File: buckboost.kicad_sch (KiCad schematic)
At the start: 17 parts, among them Q1 AO3401A, Q2 AO3401A, Q3 AO3400A, Q4 AO3400A, U4 IRS2003, U5 IRS2003

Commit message: More layout adust
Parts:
- removed C14, C15: 10u, Capacitor_SMD:C_0805_2012Metric, symbol Device:C

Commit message: Routing more
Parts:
- renumbered TP5 to TP_A, TP6 to TP_B
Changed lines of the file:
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@@
 		(dnp no)
 		(fields_autoplaced yes)
-		(property "Reference" "TP5"
-			(at 158.75 80.5179 0)
+		(property "Reference" "TP_A"
+			(at 158.75 81.7879 0)
 			(effects
 				(font
@@
 			(project "JPBms2"
 				(path "/d86e471c-a8be-422d-a5d1-5a4699b7b766/0f5ad211-c4ad-40eb-a8ac-82970ee8fac9"
-					(reference "TP5")
+					(reference "TP_A")
 					(unit 1)
 				)
@@
 		(dnp no)
 		(fields_autoplaced yes)
-		(property "Reference" "TP6"
-			(at 186.69 80.5179 0)
+		(property "Reference" "TP_B"
+			(at 186.69 81.7879 0)
 			(effects
 				(font
@@
 			(project "JPBms2"
 				(path "/d86e471c-a8be-422d-a5d1-5a4699b7b766/0f5ad211-c4ad-40eb-a8ac-82970ee8fac9"
-					(reference "TP6")
-					(unit 1)
-				)
+					(reference "TP_B")
+					(unit 1)
+				)

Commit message: Routing
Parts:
- renumbered TP_A to TP5, TP_B to TP6
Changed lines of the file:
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@@
 		(dnp no)
 		(fields_autoplaced yes)
-		(property "Reference" "TP_A"
+		(property "Reference" "TP5"
 			(at 158.75 81.7879 0)
 			(effects
@@
 				)
 				(justify left)
-				(hide yes)
 			)
 		)
@@
 			(project "JPBms2"
 				(path "/d86e471c-a8be-422d-a5d1-5a4699b7b766/0f5ad211-c4ad-40eb-a8ac-82970ee8fac9"
-					(reference "TP_A")
+					(reference "TP5")
 					(unit 1)
 				)
@@
 		(dnp no)
 		(fields_autoplaced yes)
-		(property "Reference" "TP_B"
+		(property "Reference" "TP6"
 			(at 186.69 81.7879 0)
 			(effects
@@
 				)
 				(justify left)
-				(hide yes)
 			)
 		)
@@
 			(project "JPBms2"
 				(path "/d86e471c-a8be-422d-a5d1-5a4699b7b766/0f5ad211-c4ad-40eb-a8ac-82970ee8fac9"
-					(reference "TP_B")
-					(unit 1)
-				)
+					(reference "TP6")
+					(unit 1)
+				)

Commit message: Assigning PNs
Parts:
- L1: value 220uH -> 22uH; LCSC_Code (none) -> C497873
- Q1, Q2: LCSC_Code (none) -> C15127
- Q3, Q4: LCSC_Code (none) -> C20917
- R11, R12, R13, R14: value 50 -> 75; LCSC_Code (none) -> C4275
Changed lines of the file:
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@@
 			)
 		)
-		(property "Value" "50"
+		(property "Value" "75"
 			(at 77.47 105.41 90)
 			(effects
@@
 			)
 		)
+		(property "LCSC_Code" "C4275"
+			(at 77.47 109.22 0)
+			(effects
+				(font
+					(size 1.27 1.27)
+				)
+				(hide yes)
+			)
+		)
 		(pin "1"
 		)
@@
 			)
 		)
-		(property "Value" "220uH"
+		(property "Value" "22uH"
 			(at 170.18 82.55 90)
 			(effects
@@
 			)
 		)
+		(property "LCSC_Code" "C497873"
+			(at 170.18 85.09 0)
+			(effects
+				(font
+					(size 1.27 1.27)
+				)
+				(hide yes)
+			)
+		)
 		(pin "2"
 		)
@@
 			)
 		)
-		(property "Value" "50"
+		(property "Value" "75"
 			(at 77.47 49.53 90)
 			(effects
@@
 			)
 		)
+		(property "LCSC_Code" "C4275"
+			(at 77.47 53.34 0)
+			(effects
+				(font
+					(size 1.27 1.27)
+				)
+				(hide yes)
+			)
+		)
 		(pin "1"
 		)
@@
 			)
 		)
+		(property "LCSC_Code" "C20917"
+			(at 142.24 93.98 0)
+			(effects
+				(font
+					(size 1.27 1.27)
+				)
+				(hide yes)
+			)
+		)
 		(pin "2"
 		)
@@
 			)
 		)
-		(property "Value" "50"
+		(property "Value" "75"
 			(at 77.47 118.11 90)
 			(effects
@@
 			)
 		)
+		(property "LCSC_Code" "C4275"
+			(at 77.47 121.92 0)
+			(effects
+				(font
+					(size 1.27 1.27)
+				)
+				(hide yes)
+			)
+		)
 		(pin "1"
 		)
@@
 			)
 		)
+		(property "LCSC_Code" "C15127"
+			(at 194.31 73.66 0)
+			(effects
+				(font
+					(size 1.27 1.27)
+				)
+				(hide yes)
+			)
+		)
 		(pin "3"
 		)
@@
 			)
 		)
+		(property "LCSC_Code" "C15127"
+			(at 142.24 73.66 0)
+			(effects
+				(font
+					(size 1.27 1.27)
+				)
+				(hide yes)
+			)
+		)
 		(pin "3"
 		)
@@
 			)
 		)
+		(property "LCSC_Code" "C20917"
+			(at 194.31 93.98 0)
+			(effects
+				(font
+					(size 1.27 1.27)
+				)
+				(hide yes)
+			)
+		)
 		(pin "2"
 		)
@@
 			)
 		)
-		(property "Value" "50"
+		(property "Value" "75"
 			(at 77.47 62.23 90)
 			(effects
@@
 			(at 77.47 66.04 0)
 			(effects
+				(font
+					(size 1.27 1.27)
+				)
+				(hide yes)
+			)
+		)
+		(property "LCSC_Code" "C4275"
+			(at 77.47 66.04 0)
+			(effects

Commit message: slight changes
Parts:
- C16, C17: value .1u -> 1u; LCSC_Code C14663 -> C15849
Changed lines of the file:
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@@
 		(fields_autoplaced yes)
 		(property "Reference" "C17"
-			(at 44.45 99.0537 90)
-			(effects
-				(font
-					(size 1.27 1.27)
-				)
-			)
-		)
-		(property "Value" ".1u"
-			(at 46.99 99.0537 90)
-			(effects
-				(font
-					(size 1.27 1.27)
-				)
+			(at 53.34 97.7835 0)
+			(effects
+				(font
+					(size 1.27 1.27)
+				)
+				(justify right)
+			)
+		)
+		(property "Value" "1u"
+			(at 53.34 100.3235 0)
+			(effects
+				(font
+					(size 1.27 1.27)
+				)
+				(justify right)
 			)
 		)
@@
 			)
 		)
-		(property "LCSC_Code" "C14663"
+		(property "LCSC_Code" "C15849"
 			(at 50.8 99.06 0)
 			(effects
@@
 			)
 		)
-		(property "Value" ".1u"
+		(property "Value" "1u"
 			(at 45.72 43.1737 90)
 			(effects
@@
 			)
 		)
-		(property "LCSC_Code" "C14663"
+		(property "LCSC_Code" "C15849"
 			(at 49.53 43.18 0)
 			(effects

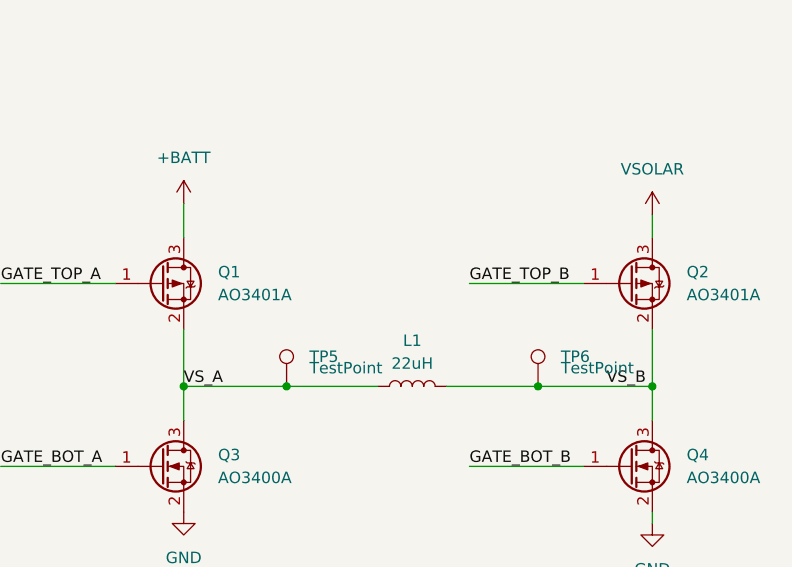
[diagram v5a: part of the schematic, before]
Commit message: Schematics updated P mosfets
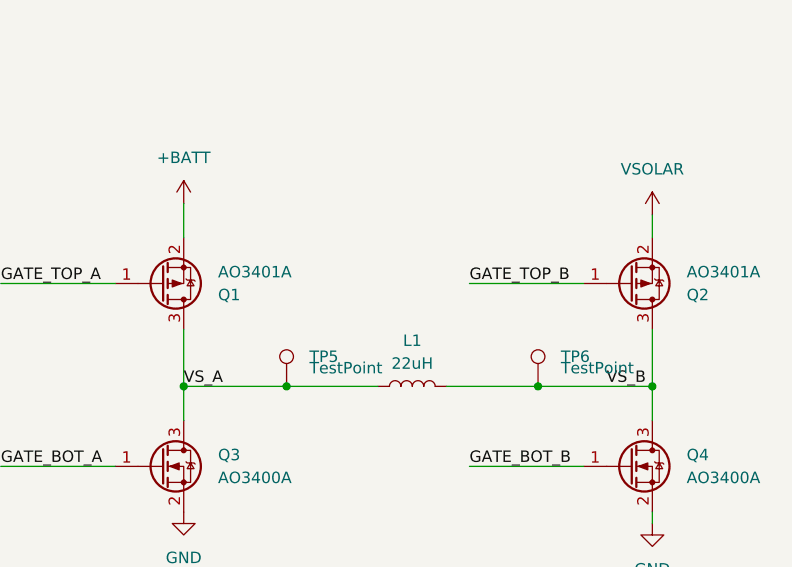
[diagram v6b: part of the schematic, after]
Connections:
- net +BATT: now also Q1.2 (S); no longer Q1.3 (D)
- net VSOLAR: now also Q2.2 (S); no longer Q2.3 (D)
- net VS_A: now also Q1.3 (D); no longer Q1.2 (S)
- net VS_B: now also Q2.3 (D); no longer Q2.2 (S)
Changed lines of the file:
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@@
 		(lib_id "Transistor_FET:AO3401A")
 		(at 194.31 73.66 0)
+		(mirror x)
 		(unit 1)
 		(exclude_from_sim no)
@@
 		(on_board yes)
 		(dnp no)
-		(fields_autoplaced yes)
 		(property "Reference" "Q2"
-			(at 200.66 72.3899 0)
+			(at 200.66 74.9301 0)
 			(effects
 				(font
@@
 		)
 		(property "Value" "AO3401A"
-			(at 200.66 74.9299 0)
+			(at 200.66 72.3901 0)
 			(effects
 				(font
@@
 		)
 		(property "Footprint" "Package_TO_SOT_SMD:SOT-23"
-			(at 199.39 75.565 0)
+			(at 199.39 71.755 0)
 			(effects
 				(font
@@
 		)
 		(property "Datasheet" "http://www.aosmd.com/pdfs/datasheet/AO3401A.pdf"
-			(at 199.39 77.47 0)
+			(at 199.39 69.85 0)
 			(effects
 				(font
@@
 		(lib_id "Transistor_FET:AO3401A")
 		(at 142.24 73.66 0)
+		(mirror x)
 		(unit 1)
 		(exclude_from_sim no)
@@
 		(on_board yes)
 		(dnp no)
-		(fields_autoplaced yes)
 		(property "Reference" "Q1"
-			(at 148.59 72.3899 0)
+			(at 148.59 74.9301 0)
 			(effects
 				(font
@@
 		)
 		(property "Value" "AO3401A"
-			(at 148.59 74.9299 0)
+			(at 148.59 72.3901 0)
 			(effects
 				(font
@@
 		)
 		(property "Footprint" "Package_TO_SOT_SMD:SOT-23"
-			(at 147.32 75.565 0)
+			(at 147.32 71.755 0)
 			(effects
 				(font
@@
 		)
 		(property "Datasheet" "http://www.aosmd.com/pdfs/datasheet/AO3401A.pdf"
-			(at 147.32 77.47 0)
+			(at 147.32 69.85 0)
 			(effects
 				(font

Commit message: New design and layout
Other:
- note added: "No bootstrap circuit, we use P-Fets on the high side, so you can just use VBATT, Practically, the bootstrap would run off of the low-side switches and let you use N-FEts. But I wanted to test this idea because it would let you control the duty cycle to any range (ex. for motor drives later). And we already had the P-FETs on the BOM"
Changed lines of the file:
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@@
+		)
+	)
+	(text "No bootstrap circuit, we use P-Fets on the high side, so you can just use VBATT,\n\nPractically, the bootstrap would run off of the low-side switches and let\nyou use N-FEts. But I wanted to test this idea because it would let you\ncontrol the duty cycle to any range (ex. for motor drives later).\nAnd we already had the P-FETs on the BOM"
+		(exclude_from_sim no)
+		(at 110.998 37.084 0)
+		(effects
+			(font
+				(size 1.27 1.27)
+			)
 		)
 	)

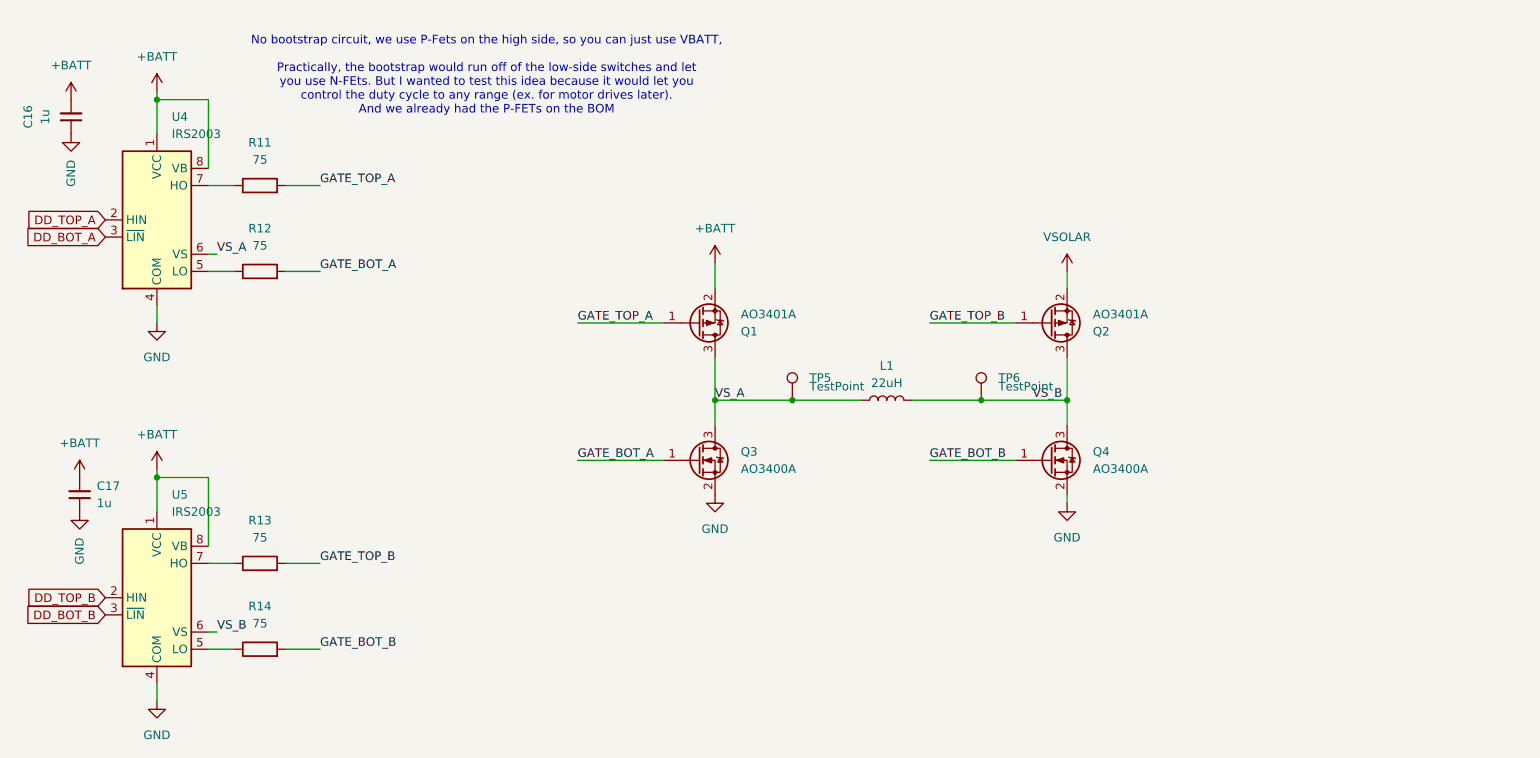
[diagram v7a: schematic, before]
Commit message: Better balance resistors, fixes
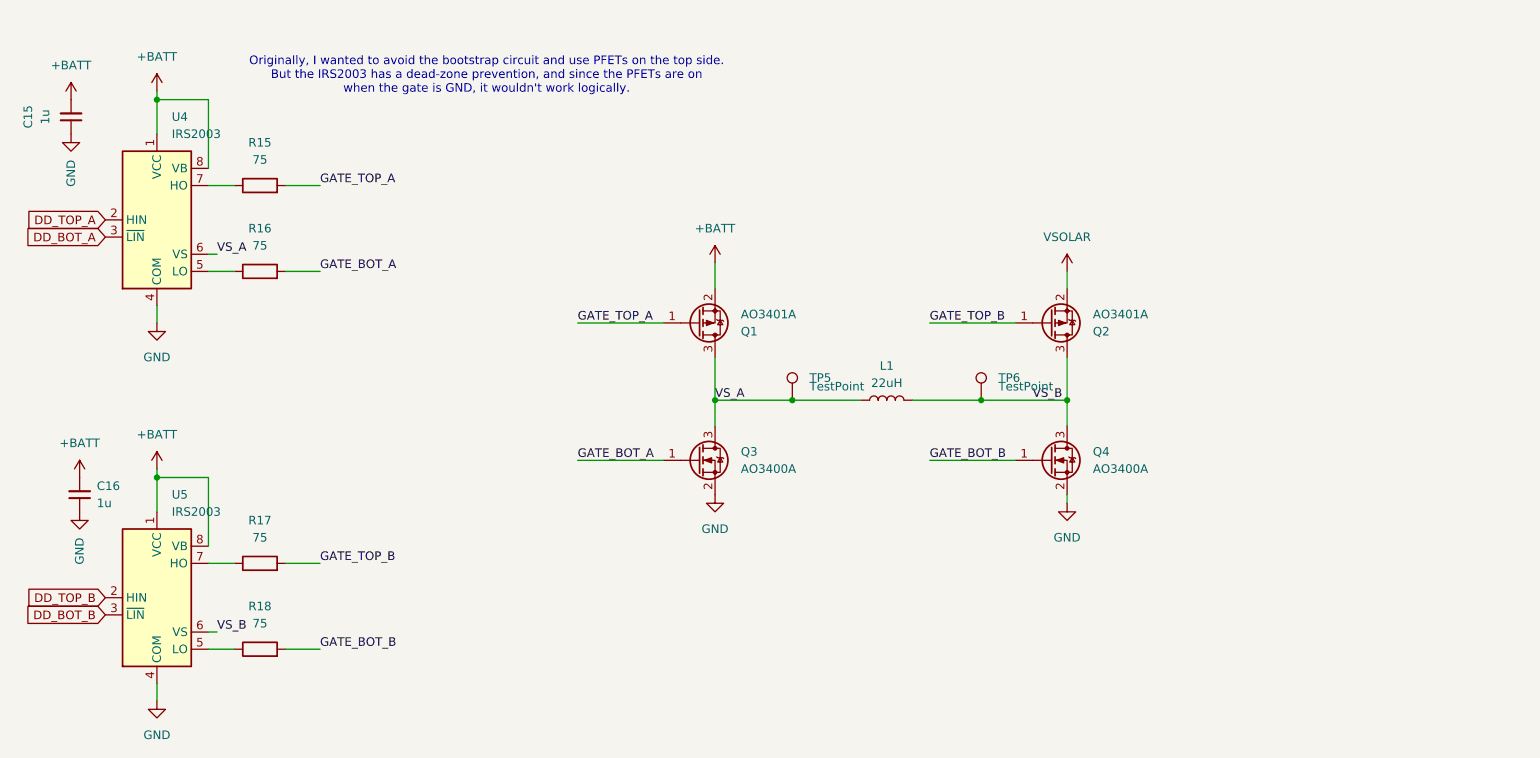
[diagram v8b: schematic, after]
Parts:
- renumbered C16 to C15, C17 to C16, R11 to R15, R12 to R16, R13 to R17, R14 to R18
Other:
- note added: "Originally, I wanted to avoid the bootstrap circuit and use PFETs on the top side. But the IRS2003 has a dead-zone prevention, and since the PFETs are on when the gate is GND, it wouldn't work logically."
- note removed: "No bootstrap circuit, we use P-Fets on the high side, so you can just use VBATT, Practically, the bootstrap would run off of the low-side switches and let you use N-FEts. But I wanted to test this idea because it would let you control the duty cycle to any range (ex. for motor drives later). And we already had the P-FETs on the BOM"
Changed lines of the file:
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@@
 		)
 	)
-	(text "No bootstrap circuit, we use P-Fets on the high side, so you can just use VBATT,\n\nPractically, the bootstrap would run off of the low-side switches and let\nyou use N-FEts. But I wanted to test this idea because it would let you\ncontrol the duty cycle to any range (ex. for motor drives later).\nAnd we already had the P-FETs on the BOM"
+	(text "Originally, I wanted to avoid the bootstrap circuit and use PFETs on the top side.\nBut the IRS2003 has a dead-zone prevention, and since the PFETs are on \nwhen the gate is GND, it wouldn't work logically."
 		(exclude_from_sim no)
 		(at 110.998 37.084 0)
@@
 		(dnp no)
 		(fields_autoplaced yes)
-		(property "Reference" "R13"
+		(property "Reference" "R17"
 			(at 77.47 102.87 90)
 			(effects
@@
 			(project "JPBms2"
 				(path "/d86e471c-a8be-422d-a5d1-5a4699b7b766/0f5ad211-c4ad-40eb-a8ac-82970ee8fac9"
-					(reference "R13")
+					(reference "R17")
 					(unit 1)
 				)
@@
 		(dnp no)
 		(fields_autoplaced yes)
-		(property "Reference" "#PWR042"
+		(property "Reference" "#PWR036"
 			(at 62.23 99.06 0)
 			(effects
@@
 			(project "JPBms2"
 				(path "/d86e471c-a8be-422d-a5d1-5a4699b7b766/0f5ad211-c4ad-40eb-a8ac-82970ee8fac9"
-					(reference "#PWR042")
+					(reference "#PWR036")
 					(unit 1)
 				)
@@
 		(dnp no)
 		(fields_autoplaced yes)
-		(property "Reference" "#PWR040"
+		(property "Reference" "#PWR032"
 			(at 49.53 52.07 0)
 			(effects
@@
 			(project "JPBms2"
 				(path "/d86e471c-a8be-422d-a5d1-5a4699b7b766/0f5ad211-c4ad-40eb-a8ac-82970ee8fac9"
-					(reference "#PWR040")
+					(reference "#PWR032")
 					(unit 1)
 				)
@@
 		(dnp no)
 		(fields_autoplaced yes)
-		(property "Reference" "#PWR030"
+		(property "Reference" "#PWR035"
 			(at 62.23 80.01 0)
 			(effects
@@
 			(project "JPBms2"
 				(path "/d86e471c-a8be-422d-a5d1-5a4699b7b766/0f5ad211-c4ad-40eb-a8ac-82970ee8fac9"
-					(reference "#PWR030")
+					(reference "#PWR035")
 					(unit 1)
 				)
@@
 		(dnp no)
 		(fields_autoplaced yes)
-		(property "Reference" "C17"
+		(property "Reference" "C16"
 			(at 53.34 97.7835 0)
 			(effects
@@
 			(project "JPBms2"
 				(path "/d86e471c-a8be-422d-a5d1-5a4699b7b766/0f5ad211-c4ad-40eb-a8ac-82970ee8fac9"
-					(reference "C17")
+					(reference "C16")
 					(unit 1)
 				)
@@
 		(dnp no)
 		(fields_autoplaced yes)
-		(property "Reference" "#PWR041"
+		(property "Reference" "#PWR037"
 			(at 50.8 100.33 0)
 			(effects
@@
 			(project "JPBms2"
 				(path "/d86e471c-a8be-422d-a5d1-5a4699b7b766/0f5ad211-c4ad-40eb-a8ac-82970ee8fac9"
-					(reference "#PWR041")
+					(reference "#PWR037")
 					(unit 1)
 				)
@@
 		(dnp no)
 		(fields_autoplaced yes)
-		(property "Reference" "#PWR034"
+		(property "Reference" "#PWR038"
 			(at 144.78 105.41 0)
 			(effects
@@
 			(project "JPBms2"
 				(path "/d86e471c-a8be-422d-a5d1-5a4699b7b766/0f5ad211-c4ad-40eb-a8ac-82970ee8fac9"
-					(reference "#PWR034")
+					(reference "#PWR038")
 					(unit 1)
 				)
@@
 		(dnp no)
 		(fields_autoplaced yes)
-		(property "Reference" "#PWR031"
+		(property "Reference" "#PWR030"
 			(at 62.23 43.18 0)
 			(effects
@@
 			(project "JPBms2"
 				(path "/d86e471c-a8be-422d-a5d1-5a4699b7b766/0f5ad211-c4ad-40eb-a8ac-82970ee8fac9"
-					(reference "#PWR031")
+					(reference "#PWR030")
 					(unit 1)
 				)
@@
 		(dnp no)
 		(fields_autoplaced yes)
-		(property "Reference" "#PWR045"
+		(property "Reference" "#PWR040"
 			(at 50.8 107.95 0)
 			(effects
@@
 			(project "JPBms2"
 				(path "/d86e471c-a8be-422d-a5d1-5a4699b7b766/0f5ad211-c4ad-40eb-a8ac-82970ee8fac9"
-					(reference "#PWR045")
+					(reference "#PWR040")
 					(unit 1)
 				)
@@
 		(dnp no)
 		(fields_autoplaced yes)
-		(property "Reference" "#PWR043"
+		(property "Reference" "#PWR041"
 			(at 62.23 135.89 0)
 			(effects
@@
 			(project "JPBms2"
 				(path "/d86e471c-a8be-422d-a5d1-5a4699b7b766/0f5ad211-c4ad-40eb-a8ac-82970ee8fac9"
-					(reference "#PWR043")
+					(reference "#PWR041")
 					(unit 1)
 				)
@@
 		(dnp no)
 		(fields_autoplaced yes)
-		(property "Reference" "R11"
+		(property "Reference" "R15"
 			(at 77.47 46.99 90)
 			(effects
@@
 			(project "JPBms2"
 				(path "/d86e471c-a8be-422d-a5d1-5a4699b7b766/0f5ad211-c4ad-40eb-a8ac-82970ee8fac9"
-					(reference "R11")
+					(reference "R15")
 					(unit 1)
 				)
@@
 		(dnp no)
 		(fields_autoplaced yes)
-		(property "Reference" "C16"
+		(property "Reference" "C15"
 			(at 43.18 43.1737 90)
 			(effects
@@
 			(project "JPBms2"
 				(path "/d86e471c-a8be-422d-a5d1-5a4699b7b766/0f5ad211-c4ad-40eb-a8ac-82970ee8fac9"
-					(reference "C16")
+					(reference "C15")
 					(unit 1)
 				)
@@
 		(dnp no)
 		(fields_autoplaced yes)
-		(property "Reference" "#PWR032"
+		(property "Reference" "#PWR033"
 			(at 144.78 68.58 0)
 			(effects
@@
 			(project "JPBms2"
 				(path "/d86e471c-a8be-422d-a5d1-5a4699b7b766/0f5ad211-c4ad-40eb-a8ac-82970ee8fac9"
-					(reference "#PWR032")
+					(reference "#PWR033")
 					(unit 1)
 				)
@@
 		(dnp no)
 		(fields_autoplaced yes)
-		(property "Reference" "R14"
+		(property "Reference" "R18"
 			(at 77.47 115.57 90)
 			(effects
@@
 			(project "JPBms2"
 				(path "/d86e471c-a8be-422d-a5d1-5a4699b7b766/0f5ad211-c4ad-40eb-a8ac-82970ee8fac9"
-					(reference "R14")
+					(reference "R18")
 					(unit 1)
 				)
@@
 		(dnp no)
 		(fields_autoplaced yes)
-		(property "Reference" "#PWR044"
+		(property "Reference" "#PWR031"
 			(at 49.53 44.45 0)
 			(effects
@@
 			(project "JPBms2"
 				(path "/d86e471c-a8be-422d-a5d1-5a4699b7b766/0f5ad211-c4ad-40eb-a8ac-82970ee8fac9"
-					(reference "#PWR044")
+					(reference "#PWR031")
 					(unit 1)
 				)
@@
 		(dnp no)
 		(fields_autoplaced yes)
-		(property "Reference" "#PWR035"
+		(property "Reference" "#PWR039"
 			(at 196.85 106.68 0)
 			(effects
@@
 			(project "JPBms2"
 				(path "/d86e471c-a8be-422d-a5d1-5a4699b7b766/0f5ad211-c4ad-40eb-a8ac-82970ee8fac9"
-					(reference "#PWR035")
+					(reference "#PWR039")
 					(unit 1)
 				)
@@
 		(dnp no)
 		(fields_autoplaced yes)
-		(property "Reference" "#PWR033"
+		(property "Reference" "#PWR034"
 			(at 196.85 69.85 0)
 			(effects
@@
 			(project "JPBms2"
 				(path "/d86e471c-a8be-422d-a5d1-5a4699b7b766/0f5ad211-c4ad-40eb-a8ac-82970ee8fac9"
-					(reference "#PWR033")
+					(reference "#PWR034")
 					(unit 1)
 				)
@@
 		(dnp no)
 		(fields_autoplaced yes)
-		(property "Reference" "R12"
+		(property "Reference" "R16"
 			(at 77.47 59.69 90)
 			(effects
@@
 			(project "JPBms2"
 				(path "/d86e471c-a8be-422d-a5d1-5a4699b7b766/0f5ad211-c4ad-40eb-a8ac-82970ee8fac9"
-					(reference "R12")
-					(unit 1)
-				)
+					(reference "R16")
+					(unit 1)
+				)
